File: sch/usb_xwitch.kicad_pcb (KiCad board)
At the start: 2 copper layers, 65 x 56.5 mm, 82 parts, among them J1 USB3_A, J2 USB3_A, J3 USB3_A, J4 USB3_A, J5 USB3_A, J6 USB3_A, J7 Raspberry_Pi_2_3, J8 Conn_01x03, J9 Conn_02x03_Odd_Even, K1 J104D2C3VDC.15S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

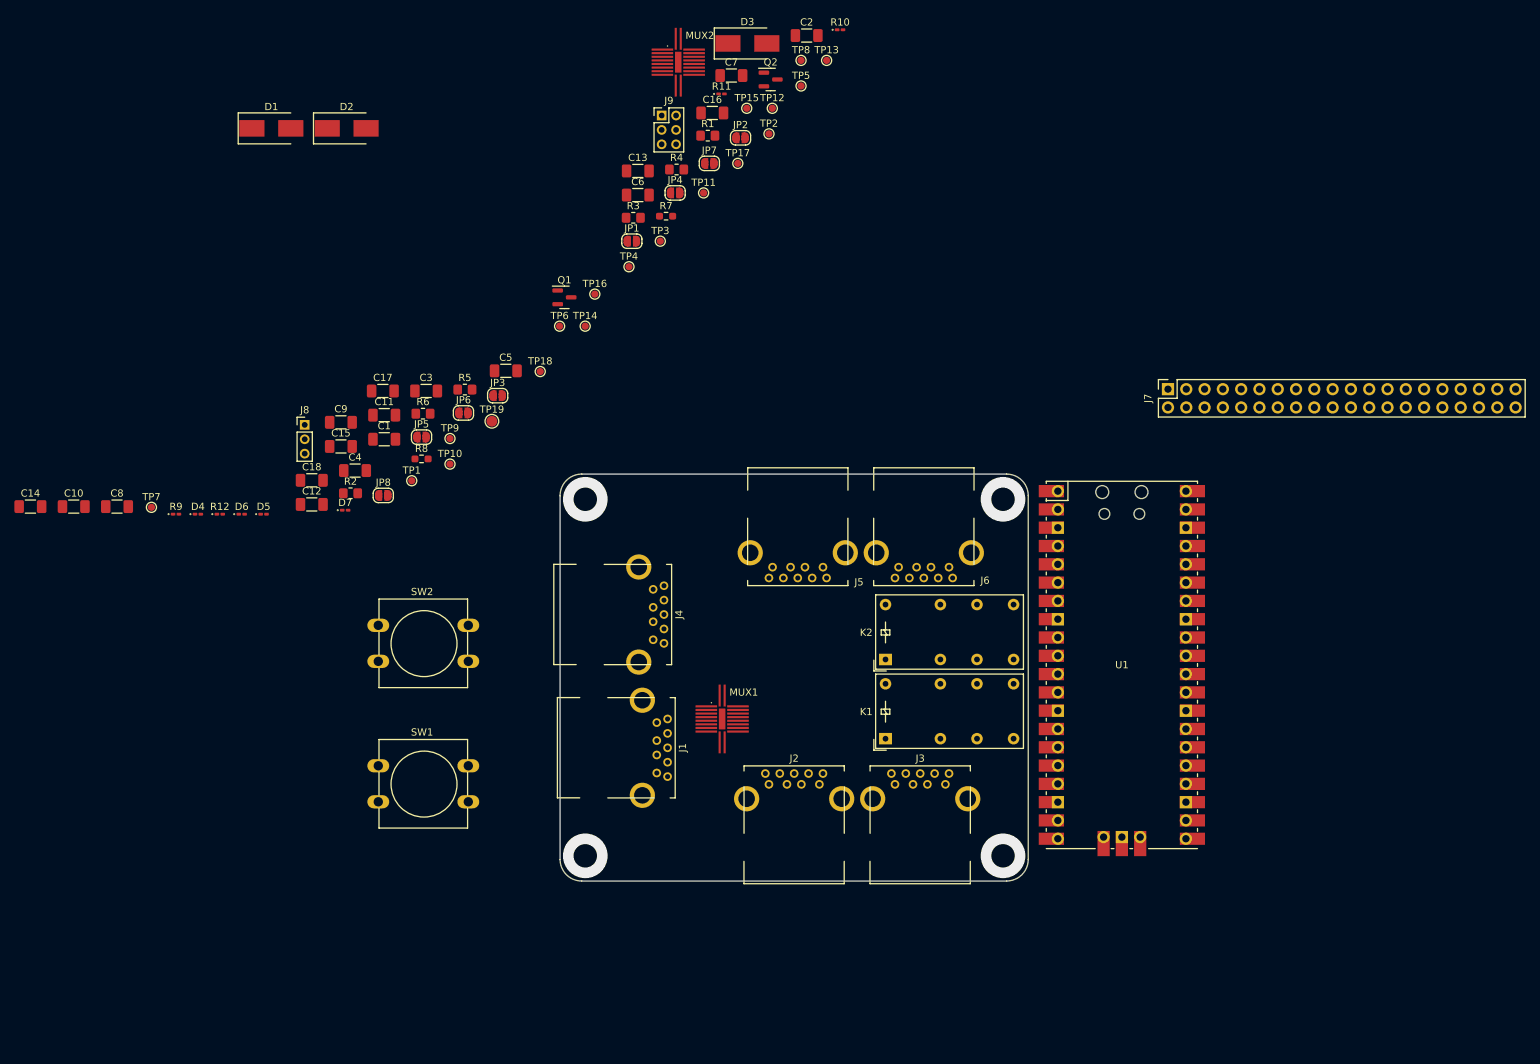
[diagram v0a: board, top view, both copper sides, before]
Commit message: changing schematics with one less mux and one more power cycle channel
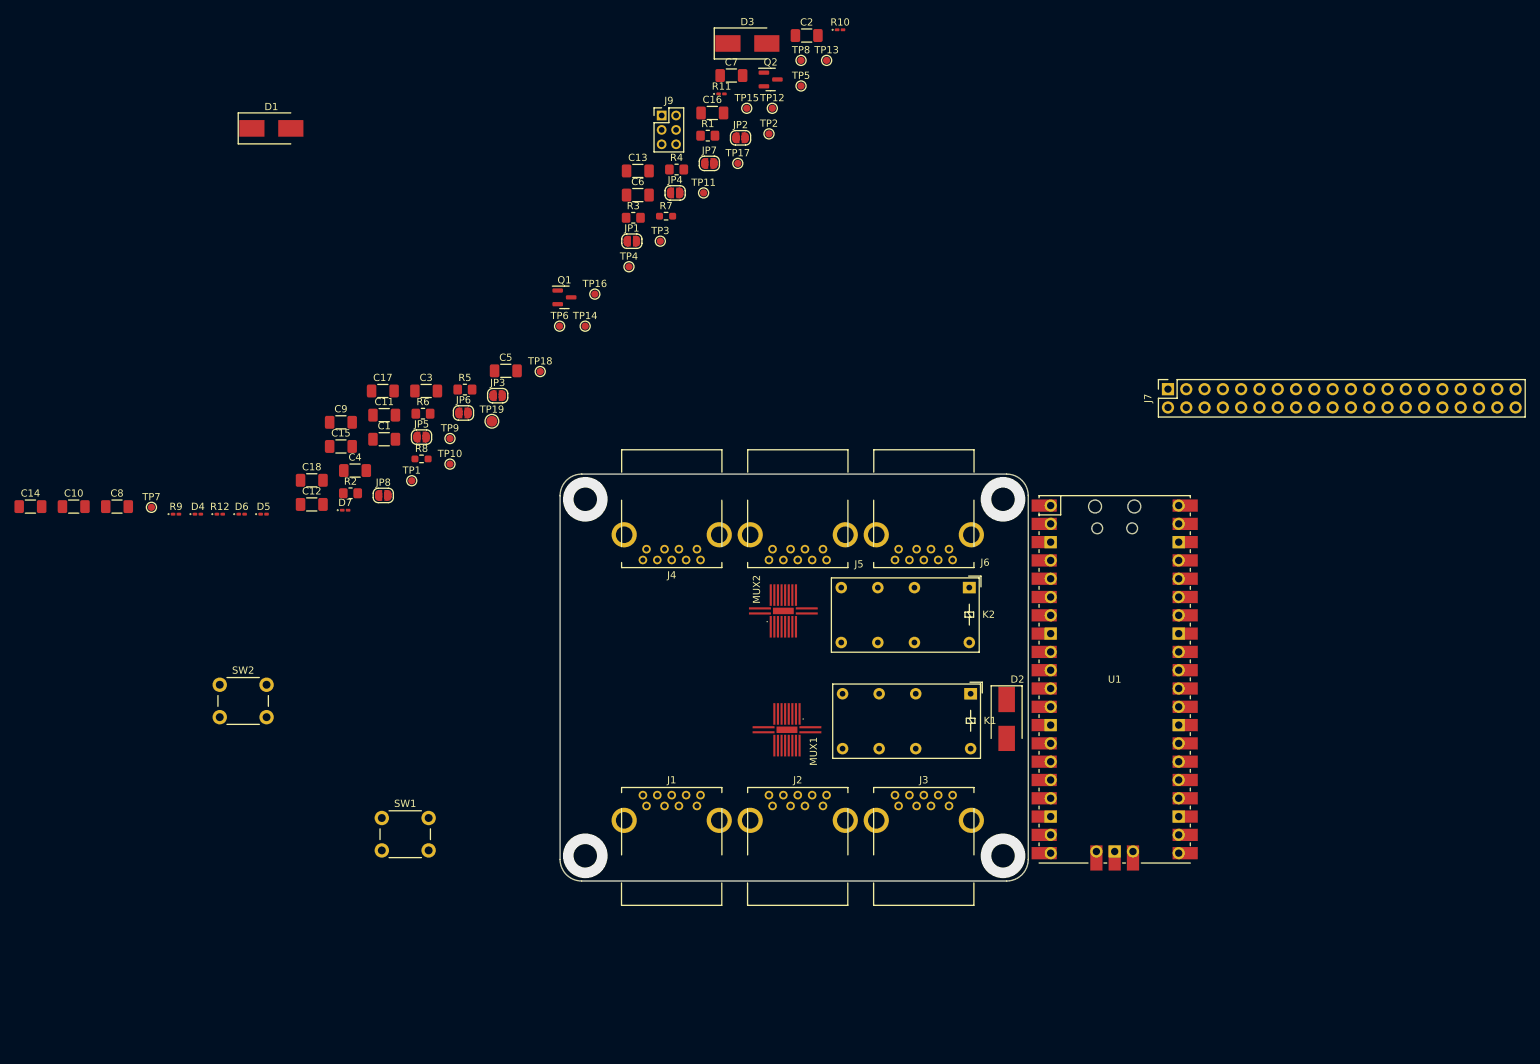
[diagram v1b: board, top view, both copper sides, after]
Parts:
- removed J8: Conn_01x03, Connector_PinHeader_2.00mm:PinHeader_1x03_P2.00mm_Vertical
- SW1, SW2: footprint Button_Switch_THT:SW_PUSH-12mm -> Button_Switch_THT:SW_PUSH_6mm
- moved D2 123.0 mm to (162.0, 114.0), turned to -90 degrees
- moved MUX2 77.6 mm to (131.0, 99.0), turned to 90 degrees
- moved SW2 23.5 mm to (52.8, 109.2)
- moved K2 15.3 mm to (156.8, 95.8), turned to 180 degrees
- moved K1 13.4 mm to (157.0, 110.5), turned to 180 degrees
- moved J1 11.7 mm to (112.0, 126.1), turned to 0 degrees
- moved MUX1 9.12 mm to (131.5, 115.5), turned to -90 degrees
- moved J4 8.25 mm to (119.0, 90.4), turned to 180 degrees
- moved SW1 7.27 mm to (75.2, 127.8)
- moved J2 3.04 mm to (129.5, 126.1)
- moved J3 3.04 mm to (147.0, 126.1)
- moved J5 2.50 mm to (136.5, 90.4)
- moved J6 2.50 mm to (154.0, 90.4)
- moved U1 2.24 mm to (177.0, 108.5)
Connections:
- U1 pad 41: Net-(J8-Pad3) -> unconnected-(U1-Pad41)
- U1 pad 42: Net-(J8-Pad2) -> unconnected-(U1-Pad42)
- U1 pad 43: Net-(J8-Pad1) -> unconnected-(U1-Pad43)

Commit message: updated rpi connector, pico footprint and board dimension
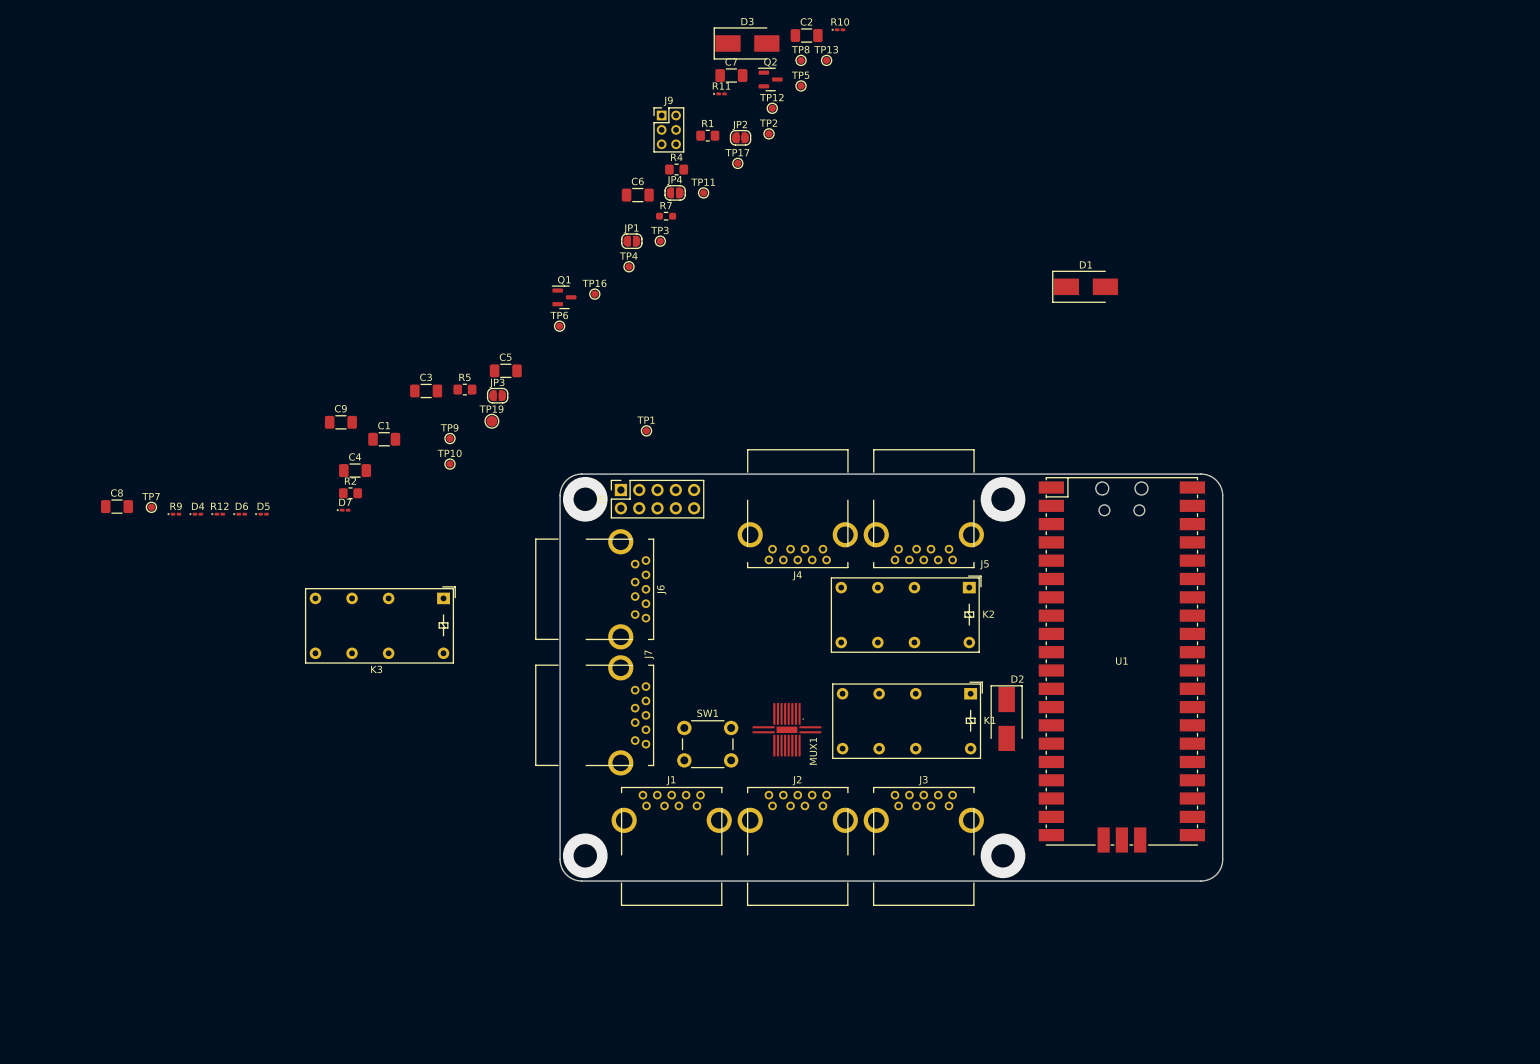
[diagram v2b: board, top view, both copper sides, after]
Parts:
- removed C10, C11, C12, C13, C14, C15, C16, C17, C18: 100n, Capacitor_SMD:C_1206_3216Metric_Pad1.33x1.80mm_HandSolder
- removed the J7 at (184.4, 68.2)
- removed JP5, JP6, JP7, JP8: SolderJumper_2_Open, Jumper:SolderJumper-2_P1.3mm_Open_RoundedPad1.0x1.5mm
- removed MUX2: PI3USB302-A, usb_xwitch:USB_MUX_DEMUX_PI3USB302-A
- removed R3: 18K, Resistor_SMD:R_0805_2012Metric_Pad1.20x1.40mm_HandSolder
- removed R6: 33K, Resistor_SMD:R_0805_2012Metric_Pad1.20x1.40mm_HandSolder
- removed R8: 10K, Resistor_SMD:R_0603_1608Metric_Pad0.98x0.95mm_HandSolder
- removed SW2: SW_MEC_5E, Button_Switch_THT:SW_PUSH_6mm
- removed TP14, TP15, TP18: TestPoint, TestPoint:TestPoint_Pad_D1.0mm
- added J6: USB3_A, usb_xwitch:USB3_A_AdamTech_USB-A3-S-RA, F.Cu at (110.4, 92.5)
- added J8: Conn_02x05_Odd_Even, Connector_PinSocket_2.54mm:PinSocket_2x05_P2.54mm_Vertical, F.Cu at (108.5, 82.2)
- added K3: J104D2C3VDC.15S, usb_xwitch:J104D2C3VDC.15S, F.Cu at (83.8, 97.3)
- U1: footprint usb_xwitch:RPi_Pico_SMD_TH -> usb_xwitch:RPi_Pico_SMD
- moved D1 115.2 mm to (173.0, 54.0)
- moved J7 47.8 mm to (110.4, 110.0), turned to -90 degrees
- moved SW1 43.8 mm to (117.2, 115.2)
- moved TP1 33.3 mm to (112.0, 74.0)
- moved J4 17.5 mm to (136.5, 90.4)
- moved J5 17.5 mm to (154.0, 90.4)
- moved U1 2.69 mm to (178.0, 106.0)
- renumbered J6 to J7
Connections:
- net /PD-B renamed Net-(TP4-Pad1)
- net /SEL-B renamed Net-(TP5-Pad1)
- D1 pad 2: Net-(D1-Pad2) -> Net-(J8-Pad4)
- J4 pad 5: /B-RX-BP -> Net-(J4-Pad5)
- J4 pad 6: /B-RX+BP -> Net-(J4-Pad6)
- J4 pad 8: /B-TX-BP -> Net-(J4-Pad8)
- J4 pad 9: /B-TX+BP -> Net-(J4-Pad9)
- J5 pad 1: /VBUS_2_1 -> Net-(J5-Pad1)
- J5 pad 5: /B-RX-BP1 -> Net-(J4-Pad5)
- J5 pad 6: /B-RX+BP1 -> Net-(J4-Pad6)
- J5 pad 8: /B-TX-BP1 -> Net-(J4-Pad8)
- J5 pad 9: /B-TX+BP1 -> Net-(J4-Pad9)
- J7 pad 1: /VBUS_2_2 -> unconnected-(J7-Pad1)
- J7 pad 10: Net-(J6-Pad10) -> Net-(J7-Pad10)
- J7 pad 2: Net-(J4-Pad2) -> unconnected-(J7-Pad2)
- J7 pad 3: Net-(J4-Pad3) -> unconnected-(J7-Pad3)
- J7 pad 4: Net-(J6-Pad10) -> Net-(J7-Pad10)
- J7 pad 5: Net-(C15-Pad2) -> unconnected-(J7-Pad5)
- J7 pad 6: Net-(C16-Pad2) -> unconnected-(J7-Pad6)
- J7 pad 7: Net-(J6-Pad10) -> Net-(J7-Pad10)
- J7 pad 8: Net-(C17-Pad2) -> unconnected-(J7-Pad8)
- J7 pad 9: Net-(C18-Pad2) -> unconnected-(J7-Pad9)
- K2 pad 14: Net-(J6-Pad10) -> unconnected-(K2-Pad14)
- K2 pad 22: /VBUS_2_1 -> Net-(J5-Pad1)
- K2 pad 24: /VBUS_2_2 -> unconnected-(K2-Pad24)
- R11 pad 1: /VBUS_2_1 -> unconnected-(R11-Pad1)
- R12 pad 1: /VBUS_2_2 -> unconnected-(R12-Pad1)
- TP1 pad 1: Net-(D1-Pad2) -> +5V
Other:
- board size 65 x 56.5 mm -> 92 x 56.5 mm

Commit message: updated 3d model and pcb, sch finalize
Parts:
- added D8: VS-10BQ015, Diode_SMD:D_SMB_Handsoldering, F.Cu at (127.5, 108.5)
- added Q3: 2N7002P, Package_TO_SOT_SMD:SOT-23, F.Cu at (115.2, 21.9)
- moved C8 130.4 mm to (145.5, 159.0)
- moved C7 130.3 mm to (149.0, 152.5)
- moved C2 130.0 mm to (128.5, 149.0)
- moved C6 113.6 mm to (140.0, 151.0)
- moved C5 95.9 mm to (144.0, 146.5)
- moved C3 95.1 mm to (124.0, 153.5)
- moved J9 94.6 mm to (102.0, 124.1)
- moved C4 93.6 mm to (121.0, 159.0)
- moved D3 86.9 mm to (161.5, 99.5), turned to -90 degrees
- moved C1 84.7 mm to (125.0, 144.0)
- moved D1 64.6 mm to (119.0, 89.5), turned to 180 degrees
- moved K3 42.0 mm to (123.2, 111.8), turned to 90 degrees
- moved MUX1 2.06 mm to (132.0, 117.5)
- moved D2 0.50 mm to (161.5, 114.0)
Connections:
- J5 pad 1: Net-(J5-Pad1) -> /VBUS2
- J6 pad 1: unconnected-(J6-Pad1) -> Net-(K3-Pad21)
- J6 pad 2: unconnected-(J6-Pad2) -> Net-(J6-Pad2)
- J6 pad 3: unconnected-(J6-Pad3) -> Net-(J6-Pad3)
- J6 pad 5: unconnected-(J6-Pad5) -> Net-(J6-Pad5)
- J6 pad 6: unconnected-(J6-Pad6) -> Net-(J6-Pad6)
- J6 pad 8: unconnected-(J6-Pad8) -> Net-(J6-Pad8)
- J6 pad 9: unconnected-(J6-Pad9) -> Net-(J6-Pad9)
- J7 pad 1: unconnected-(J7-Pad1) -> /VBUS3
- J7 pad 10: Net-(J7-Pad10) -> Net-(K3-Pad12)
- J7 pad 2: unconnected-(J7-Pad2) -> Net-(J6-Pad2)
- J7 pad 3: unconnected-(J7-Pad3) -> Net-(J6-Pad3)
- J7 pad 4: Net-(J7-Pad10) -> Net-(K3-Pad12)
- J7 pad 5: unconnected-(J7-Pad5) -> Net-(J6-Pad5)
- J7 pad 6: unconnected-(J7-Pad6) -> Net-(J6-Pad6)
- J7 pad 7: Net-(J7-Pad10) -> Net-(K3-Pad12)
- J7 pad 8: unconnected-(J7-Pad8) -> Net-(J6-Pad8)
- J7 pad 9: unconnected-(J7-Pad9) -> Net-(J6-Pad9)
- K2 pad 22: Net-(J5-Pad1) -> /VBUS2
- K3 pad 11: unconnected-(K3-Pad11) -> GND
- K3 pad 12: unconnected-(K3-Pad12) -> Net-(K3-Pad12)
- K3 pad 21: unconnected-(K3-Pad21) -> Net-(K3-Pad21)
- K3 pad 22: unconnected-(K3-Pad22) -> /VBUS3
- K3 pad A1: unconnected-(K3-PadA1) -> +5V
- K3 pad A2: unconnected-(K3-PadA2) -> /RL3
- R11 pad 1: unconnected-(R11-Pad1) -> /VBUS2
- R12 pad 1: unconnected-(R12-Pad1) -> /VBUS3
- TP6 pad 1: /REL-B -> /REL-C
- TP7 pad 1: /SW-B -> /REL-B
- U1 pad 26: /REL-B -> /REL-C
- U1 pad 27: /SW-B -> /REL-B
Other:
- board text added: "RNL USB-XWitch"

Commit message: updated pcb
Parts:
- moved Q1 89.1 mm to (161.5, 120.5), turned to 180 degrees
- moved Q2 87.0 mm to (161.5, 106.0), turned to 180 degrees
- moved Q3 81.0 mm to (127.5, 102.0)
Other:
- board text added: "RNL USB-Xwitch v0.1"
- board text removed: "RNL USB-XWitch"

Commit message: pcb update
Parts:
- C1, C2, C3, C4, C5, C6, C7, C8: footprint Capacitor_SMD:C_1206_3216Metric_Pad1.33x1.80mm_HandSolder -> Capacitor_SMD:C_0805_2012Metric_Pad1.18x1.45mm_HandSolder; moved to B.Cu
- C9, JP1, JP2, JP3, JP4, R1, R2, R4, R5, R7: moved to B.Cu
- moved R10 113.7 mm to (141.8, 132.0), turned to -90 degrees
- moved R2 109.4 mm to (178.5, 102.5)
- moved R5 102.1 mm to (183.0, 102.5)
- moved JP2 98.7 mm to (126.2, 132.0)
- moved D5 96.0 mm to (141.8, 134.0), turned to 90 degrees
- moved R4 94.5 mm to (183.0, 104.5)
- moved JP4 93.8 mm to (122.5, 134.5)
- moved R1 92.1 mm to (178.5, 104.5)
- moved R9 90.4 mm to (124.2, 132.0), turned to -90 degrees
- moved D4 88.9 mm to (124.2, 134.0), turned to 90 degrees
- moved JP1 88.3 mm to (126.2, 134.5)
- moved D6 86.0 mm to (141.8, 82.5), turned to -90 degrees
- moved R7 76.3 mm to (115.0, 120.5), turned to 90 degrees
- moved C9 71.8 mm to (126.5, 116.5), turned to -90 degrees
- moved JP3 70.2 mm to (122.5, 132.0)
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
